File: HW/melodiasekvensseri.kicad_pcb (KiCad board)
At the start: 2 copper layers, 60.6 x 110 mm, 58 parts, among them IC1 74LS138, J1 Conn_02x05_Odd_Even, J2 Clock_In, J3 Gate_Out, J4 CV_Out, J5 Conn_02x03_Odd_Even, J6 Conn_01x04, U1 TLV2372IP

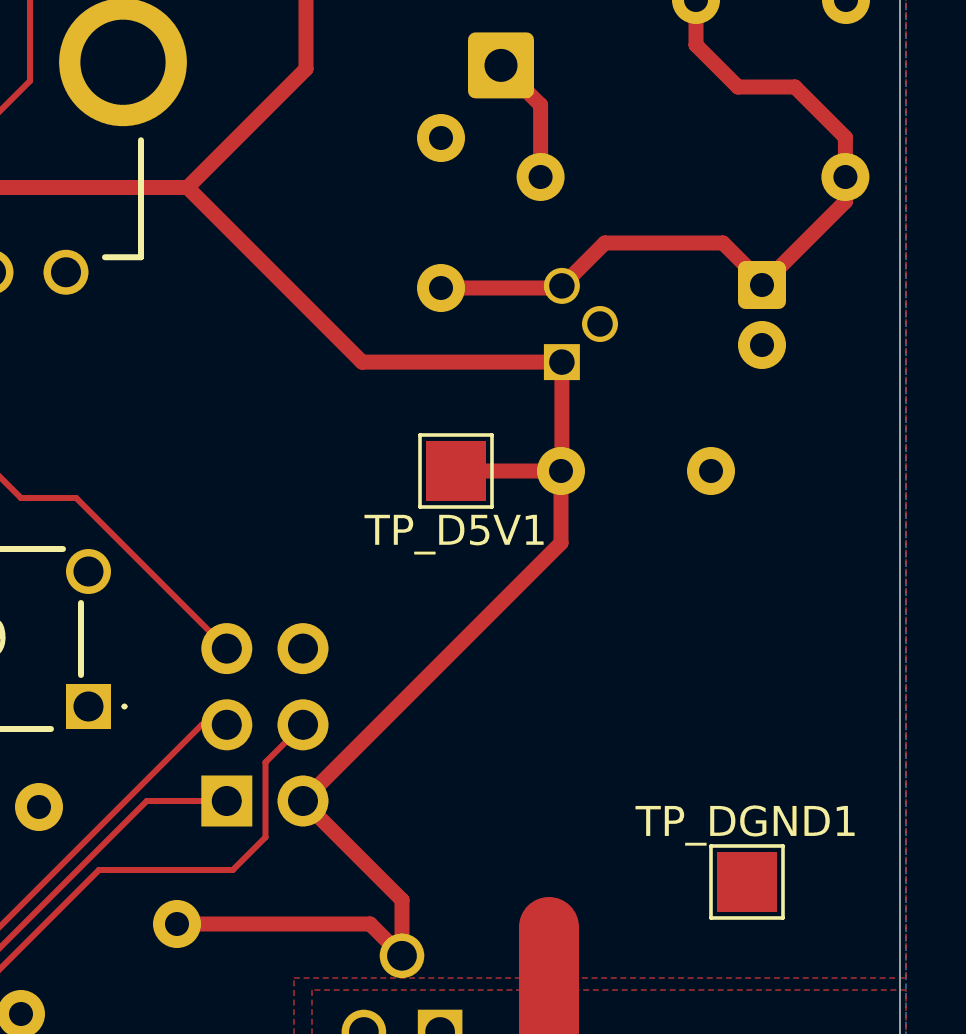
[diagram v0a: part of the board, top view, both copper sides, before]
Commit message: Panel clearances, switched REG1, added test code
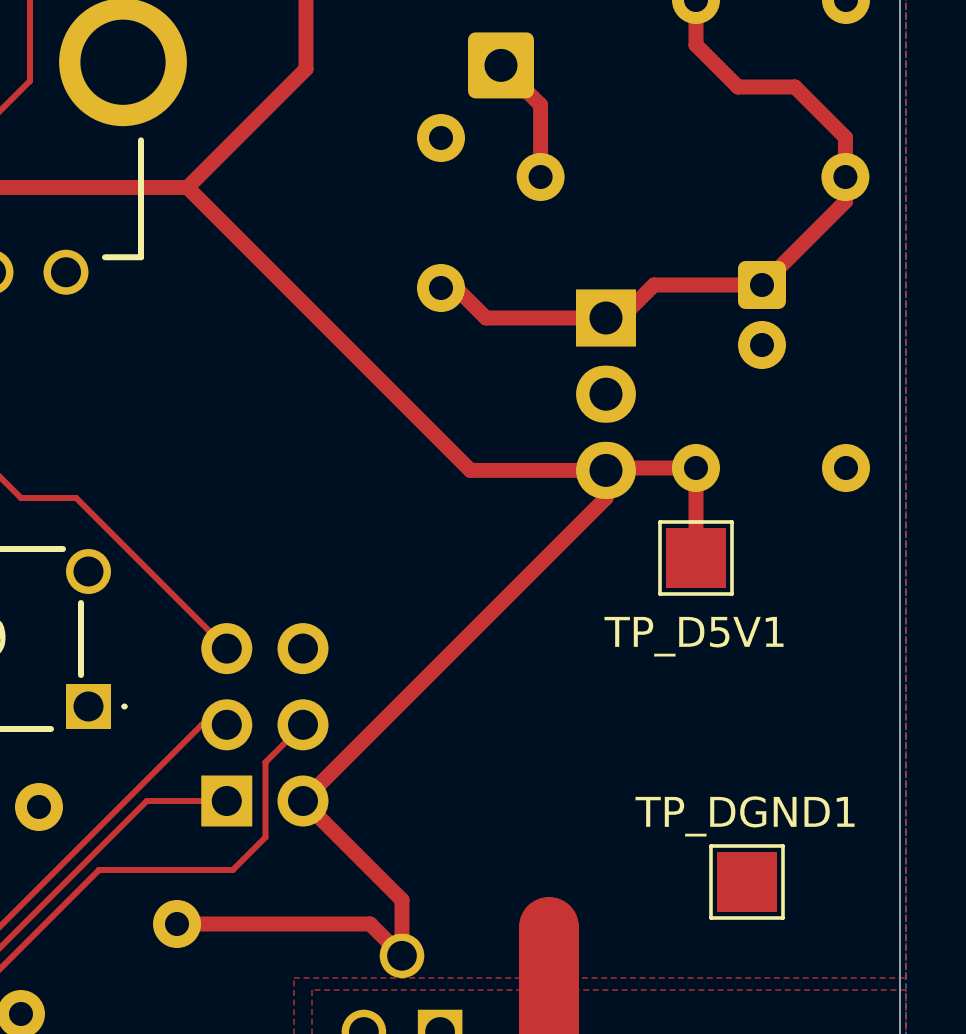
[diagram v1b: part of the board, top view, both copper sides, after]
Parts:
- REG1: footprint Project_Libraries:L78L05ACZ -> Package_TO_SOT_THT:TO-220-3_Vertical
- moved TP_D5V1 8.51 mm to (173.5, 85.5)
- moved C6 4.50 mm to (178.5, 82.5)
- moved REG1 2.08 mm to (170.5, 77.5), turned to -90 degrees
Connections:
- REG1 pad 1: D_+5V -> +12V
- REG1 pad 3: +12V -> D_+5V
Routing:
- net D_+5V: track 230.2 -> 232.7 mm

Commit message: Updated REG1 model name
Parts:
- REG1: value L78L05ACZ -> LM78M05
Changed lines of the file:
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@@
 			)
 		)
-		(property "Value" "L78L05ACZ"
-			(at 2.54 -2.2 90)
+		(property "Value" "LM78M05"
+			(at 4 2.5 90)
 			(layer "B.Fab")
 			(effects

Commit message: Removed CV_OUT diodes, filtering cap added
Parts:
- removed D4, D5: 1N4148, Diode_THT:D_DO-35_SOD27_P7.62mm_Horizontal
- added C15: 100n, Capacitor_THT:C_Disc_D5.0mm_W2.5mm_P5.00mm, B.Cu at (133.3, 97.7)
- TP_AGND1: footprint TestPoint:TestPoint_Pad_2.0x2.0mm -> TestPoint:TestPoint_THTPad_2.0x2.0mm_Drill1.0mm
- TP_CV_OUT1: renamed from TP_DAC_OUT1; footprint TestPoint:TestPoint_Pad_2.0x2.0mm -> TestPoint:TestPoint_THTPad_2.0x2.0mm_Drill1.0mm
- moved TP_A5V1 4.56 mm to (163.8, 120.7)
- moved TP_CV_OUT1 3.24 mm to (161.5, 129.8)
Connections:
- TP_CV_OUT1 pad 1: Net-(DAC1-VOUT) -> CV_Out
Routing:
- net Net-(DAC1-VOUT): track 25.2 -> 8.25 mm
- net A_+5V: track 58.8 -> 51.2 mm
- net CV_Out: track 32.1 -> 34.7 mm
- net D_+5V: track 232.7 -> 233.3 mm

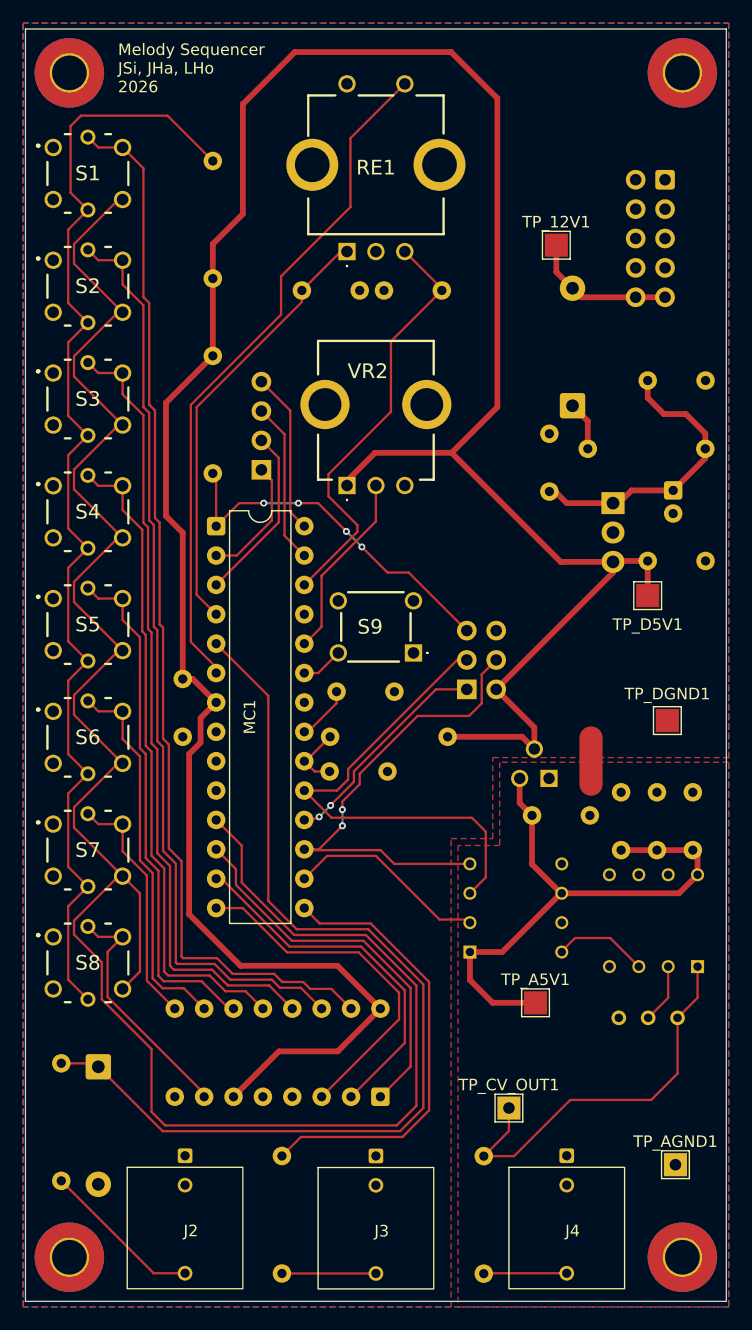
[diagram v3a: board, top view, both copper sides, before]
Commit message: Some resistor footprints changed
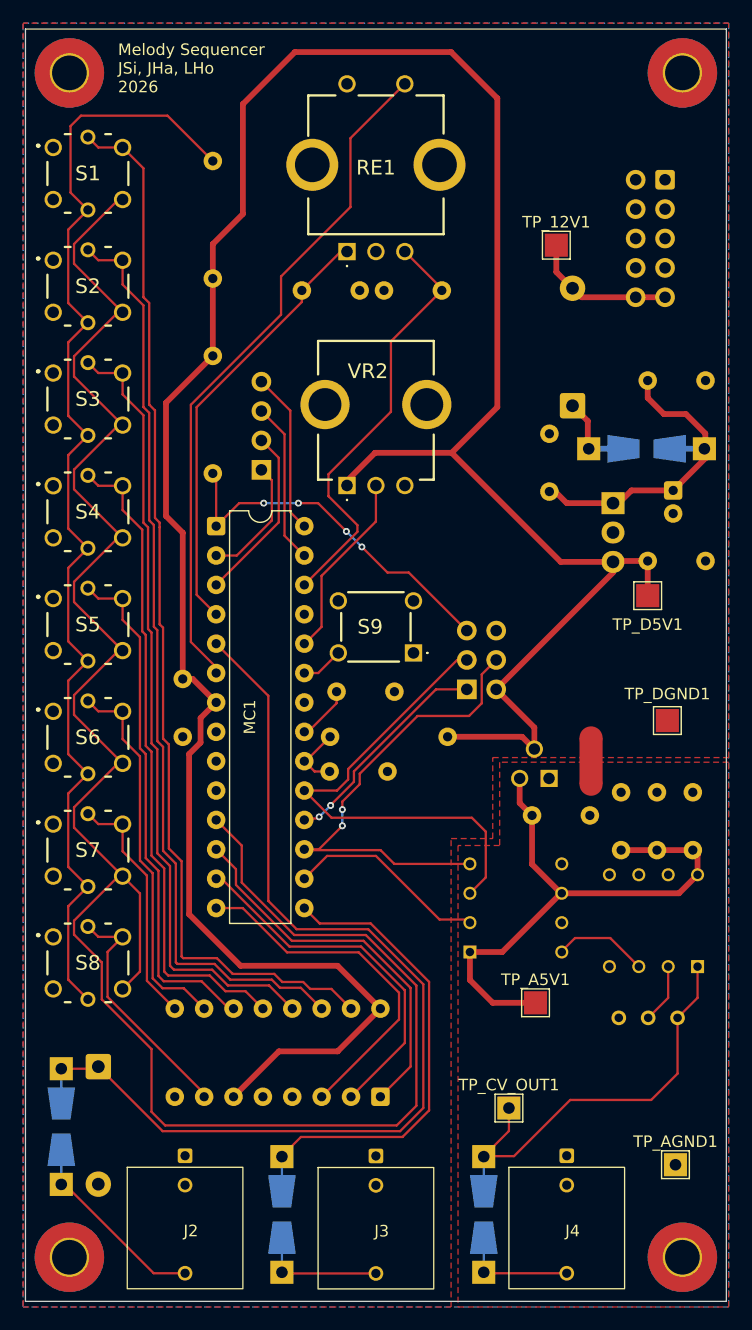
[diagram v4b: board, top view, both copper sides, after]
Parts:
- removed D3: 1N4733A, Diode_THT:D_DO-41_SOD81_P10.16mm_Horizontal
- added D2: 1N4733A, Diode_THT:D_DO-41_SOD81_P10.16mm_Horizontal, B.Cu at (126.0, 126.2)
- R1, R4, R5, R6: footprint Resistor_THT:R_Axial_DIN0207_L6.3mm_D2.5mm_P10.16mm_Horizontal -> Resistors_Universal.pretty-master:Resistor_SMD+THTuniversal_0805to1206_RM10_HandSoldering_RevA_Date25Jun2010
- moved R6 5.12 mm to (159.3, 139.0)
- moved R5 5.10 mm to (141.9, 139.0)
- moved R1 5.08 mm to (173.4, 72.8)
- moved R4 4.69 mm to (122.8, 131.4)
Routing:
- net CLK_IN: track 85.3 -> 88.7 mm
- net Net-(J4-PadT): track 7.14 -> 10.1 mm
- net Net-(J3-PadT): track 8.12 -> 11.1 mm
- net CV_Out: track 34.7 -> 37.7 mm
- net +12V: track 25.4 -> 28.4 mm
- net Net-(J2-PadT): track 14.0 -> 17.0 mm
- net Net-(D1-K): track 4.27 -> 7.27 mm
- net GATE_OUT: track 38.9 -> 41.9 mm

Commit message: REG2 changed, grounding fixes, routing changes
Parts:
- removed C7: 10u, Capacitor_THT:C_Disc_D5.0mm_W2.5mm_P5.00mm
- removed REF** (x4): MountingHole_3mm_Pad_TopBottom, MountingHole:MountingHole_3mm_Pad_TopBottom
- added C16: 100n, Capacitor_THT:C_Disc_D5.0mm_W2.5mm_P5.00mm, B.Cu at (166.5, 114.5)
- added C17: 330n, Capacitor_THT:C_Disc_D5.0mm_W2.5mm_P5.00mm, B.Cu at (166.5, 104.5)
- added H1: MountingHole, MountingHole:MountingHole_3.2mm_M3, F.Cu at (123.5, 40.3)
- added H2: MountingHole, MountingHole:MountingHole_3.2mm_M3, F.Cu at (176.5, 40.3)
- added H3: MountingHole, MountingHole:MountingHole_3.2mm_M3, F.Cu at (123.5, 142.7)
- added H4: MountingHole, MountingHole:MountingHole_3.2mm_M3, F.Cu at (176.5, 142.7)
- REG2: value MCP1700-5002E_TO -> L78L05ACZ; footprint Project_Libraries:TO127P254X495-3 -> Project_Libraries:L78L05ACZ
- TP_AGND1, TP_CV_OUT1: footprint TestPoint:TestPoint_THTPad_2.0x2.0mm_Drill1.0mm -> TestPoint:TestPoint_THTPad_1.5x1.5mm_Drill0.7mm
- moved REG2 12.1 mm to (164.1, 110.8)
- moved C5 11.3 mm to (163.3, 82.7), turned to 90 degrees
- moved TP_A5V1 10.2 mm to (161.0, 130.5)
- moved DAC1 9.00 mm to (162.1, 121.5)
- moved TP_CV_OUT1 8.51 mm to (170.0, 129.5), turned to 90 degrees
- moved TP_AGND1 6.19 mm to (172.5, 129.5), turned to -90 degrees
- moved R3 2.90 mm to (133.0, 58.1)
- moved C6 2.21 mm to (176.3, 82.7)
- moved REG1 2.21 mm to (168.3, 77.7)
- moved TP_D5V1 2.21 mm to (171.3, 85.7)
- moved J5 2.06 mm to (157.9, 91.5)
- moved R1 1.90 mm to (171.5, 72.8)
- moved R7 0.90 mm to (135.0, 74.9)
- moved C13 0.45 mm to (152.0, 94.0)
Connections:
- REG2 pad 1: A_GND -> A_+5V
- REG2 pad 2: D_+5V -> A_GND
- REG2 pad 3: A_+5V -> +12V
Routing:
- net D_+5V: track 233.3 -> 169.9 mm
- net +12V: track 28.4 -> 66.7 mm
- net D_GND: track 0.00 -> 31.7 mm, vias 0 -> 30
- net CV_Out: track 37.7 -> 30.7 mm
- net SPI_SCK: track 42.3 -> 47.7 mm, vias 0 -> 2
- net SPI_MOSI: track 41.4 -> 45.8 mm
- net DAC_CS: track 17.6 -> 21.1 mm
- net Net-(DAC1-VOUT): track 8.25 -> 11.2 mm
- net Net-(S1-A): track 100.3 -> 97.4 mm
- net Net-(IC1-O3): track 56.7 -> 54.3 mm
- net Net-(IC1-O2): track 68.4 -> 66.2 mm
- net Net-(IC1-O1): track 80.2 -> 78.1 mm
- net A_+5V: track 51.2 -> 49.2 mm
- net Net-(IC1-O0): track 92.0 -> 90.0 mm
- net Net-(IC1-O4): track 44.6 -> 42.6 mm
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- added copper zone on B.Cu, net A_GND

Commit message: Cleanup traces
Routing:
- net +12V: track 66.7 -> 65.6 mm
- net ENC_B: track 37.8 -> 36.9 mm
- net Net-(MC1-AREF): track 4.74 -> 3.92 mm
- net Net-(D1-K): track 6.93 -> 6.22 mm
- net ENC_A: track 39.1 -> 38.5 mm
- net ENC_S: track 60.2 -> 59.7 mm
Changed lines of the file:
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@@
 		(capping no)
 		(filling no)
-		(zone_defaults)
 		(pcbplotparams
 			(layerselection 0x00000000_00000000_55555555_575555ff)
@@
 	(segment
 		(start 149.675 73.4)
-		(end 156.3 73.4)
-		(width 0.5)
-		(layer "F.Cu")
-		(net "D_+5V")
-	)
-	(segment
-		(start 171.22 82.78)
-		(end 171.3 82.7)
+		(end 156.4 73.4)
 		(width 0.5)
 		(layer "F.Cu")
@@
 	)
 	(segment
-		(start 156.4 73.4)
-		(end 156.3 73.4)
-		(width 0.5)
-		(layer "F.Cu")
-		(net "D_+5V")
-	)
-	(segment
 		(start 149.675 67.775)
 		(end 149.675 73.4)
@@
 	)
 	(segment
-		(start 143.81 89.65)
-		(end 143.85 89.65)
-		(width 0.2)
-		(layer "F.Cu")
-		(net "TEMPO")
-	)
-	(segment
 		(start 152.5 111)
 		(end 152.373789 111)
@@
 	)
 	(segment
-		(start 147.5 55.75)
-		(end 146.963132 55.75)
-		(width 0.2)
-		(layer "F.Cu")
-		(net "ENC_A")
-	)
-	(segment
 		(start 133.65 72.25)
 		(end 133.65 84.57)
@@
 	)
 	(segment
-		(start 155.7 58.95)
-		(end 155.7 59.113132)
-		(width 0.2)
-		(layer "F.Cu")
-		(net "ENC_B")
-	)
-	(segment
 		(start 152.5 55.75)
 		(end 155.7 58.95)
@@
 	)
 	(segment
-		(start 152.95 55.263132)
-		(end 152.2 55.263132)
-		(width 0.2)
-		(layer "F.Cu")
-		(net "ENC_B")
-	)
-	(segment
 		(start 143.81 84.57)
 		(end 148.4 79.98)
@@
 		(net "ENC_S")
 	)
-	(segment
-		(start 136.19 91.69)
-		(end 136.19 92.19)
-		(width 0.2)
-		(layer "F.Cu")
-		(net "ENC_S")
-	)
 	(via
 		(at 137.3 62.7)
@@
 	)
 	(segment
-		(start 125.82126 126.39874)
-		(end 126 126.22)
-		(width 0.2)
-		(layer "F.Cu")
-		(net "CLK_IN")
-	)
-	(segment
 		(start 143.146566 114.33946)
 		(end 142 113.192894)
@@
 	)
 	(segment
-		(start 143.84 110)
-		(end 143.81 109.97)
-		(width 0.2)
-		(layer "F.Cu")
-		(net "DAC_CS")
-	)
-	(segment
 		(start 155.5 119)
 		(end 148 111.5)
@@
 	)
 	(segment
-		(start 160.830469 89)
-		(end 160.4 89)
-		(width 0.2)
-		(layer "F.Cu")
-		(net "SPI_MOSI")
-	)
-	(segment
 		(start 163.5 91.702083)
 		(end 163.5 94)
@@
 	)
 	(segment
-		(start 143.934975 105.014975)
-		(end 143.81 104.89)
-		(width 0.2)
-		(layer "F.Cu")
-		(net "SPI_MISO")
-	)
-	(segment
 		(start 148.5 102)
 		(end 148.5 101)
@@
 	)
 	(segment
-		(start 157.86 91.64)
-		(end 157.86 91.54)
-		(width 0.2)
-		(layer "F.Cu")
-		(net "SPI_MISO")
-	)
-	(segment
 		(start 146.5 104)
 		(end 148.5 102)
@@
 	)
 	(segment
-		(start 158.13 120.23)
-		(end 158.13 120.13)
-		(width 0.2)
-		(layer "F.Cu")
-		(net "SPI_SCK")
-	)
-	(segment
 		(start 157 89)
 		(end 155.5 90.5)
@@
 	)
 	(segment
-		(start 143.93 99.81)
-		(end 143.81 99.81)
-		(width 0.2)
-		(layer "F.Cu")
-		(net "Net-(MC1-AVCC)")
-	)
-	(segment
-		(start 143.81 97.19)
-		(end 143.81 97.27)
-		(width 0.2)
-		(layer "F.Cu")
-		(net "Net-(MC1-AREF)")
-	)
-	(segment
-		(start 143.81 97.27)
-		(end 144.13 97.27)
-		(width 0.2)
-		(layer "F.Cu")
-		(net "Net-(MC1-AREF)")
-	)
-	(segment
-		(start 146.58 94.5)
-		(end 147 94.5)
-		(width 0.2)
-		(layer "F.Cu")
-		(net "Net-(MC1-AREF)")
-	)
-	(segment
 		(start 143.81 97.27)
 		(end 146.58 94.5)
@@
 	)
 	(segment
-		(start 122.8 136.093132)
-		(end 130.79 144.083132)
-		(width 0.2)
-		(layer "F.Cu")
-		(net "Net-(J2-PadT)")
-	)
-	(segment
-		(start 130.79 144.083132)
-		(end 133.5 144.083132)
-		(width 0.2)
-		(layer "F.Cu")
-		(net "Net-(J2-PadT)")
-	)
-	(segment
-		(start 122.8 133.39898)
-		(end 122.8 136.40126)
-		(width 0.2)
-		(layer "B.Cu")
-		(net "Net-(J2-PadT)")
-	)
-	(segment
 		(start 167.5 129.5)
 		(end 163.00126 133.99874)
@@
 	)
 	(segment
+		(start 122.8 136.093132)
+		(end 130.79 144.083132)
+		(width 0.2)
+		(layer "F.Cu")
+		(net "Net-(J2-PadT)")
+	)
+	(segment
+		(start 130.79 144.083132)
+		(end 133.5 144.083132)
+		(width 0.2)
+		(layer "F.Cu")
+		(net "Net-(J2-PadT)")
+	)
+	(segment
+		(start 122.8 133.39898)
+		(end 122.8 136.40126)
+		(width 0.2)
+		(layer "B.Cu")
+		(net "Net-(J2-PadT)")
+	)
+	(segment
 		(start 137.296026 120.243689)
 		(end 137.296026 121.203132)
@@
 	)
 	(segment
-		(start 175.7 76.4)
-		(end 176.3 76.4)
-		(width 0.5)
-		(layer "F.Cu")
-		(net "+12V")
-	)
-	(segment
 		(start 173.5 78.1)
 		(end 173.5 89.2)
@@
 	)
 	(segment
-		(start 175.7 76.4)
-		(end 175.2 76.4)
-		(width 0.5)
-		(layer "F.Cu")
-		(net "+12V")
-	)
-	(segment
 		(start 173.5 66.9)
 		(end 173.5 68.4)
@@
 	)
 	(segment
-		(start 172.73 117.77)
-		(end 172.73 117.57)
-		(width 0.2)
-		(layer "F.Cu")
-		(net "Net-(DAC1-VOUT)")
-	)
-	(segment
 		(start 169 123.5)
 		(end 169 121.5)
@@
 	)
 	(segment
-		(start 167 72.29874)
-		(end 166.49874 72.8)
-		(width 0.5)
-		(layer "F.Cu")
-		(net "Net-(D1-K)")
-	)
-	(segment

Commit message: Added ground via, small changes
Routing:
- net D_GND: track 31.7 -> 33.5 mm, vias 30 -> 32
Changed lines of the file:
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@@
+	)
+	(segment
+		(start 140 125.31105)
+		(end 139.905525 125.405525)
+		(width 0.2)
+		(layer "F.Cu")
+		(net "D_GND")
 	)
 	(segment
@@
 	)
 	(via
+		(at 141.107607 126.607607)
+		(size 0.6)
+		(drill 0.3)
+		(layers "F.Cu" "B.Cu")
+		(net "D_GND")
+	)
+	(via
 		(at 139.5 79.5)
 		(size 0.6)
@@
 	(via
 		(at 152.373789 111)
+		(size 0.6)
+		(drill 0.3)
+		(layers "F.Cu" "B.Cu")
+		(net "D_GND")
+	)
+	(via
+		(at 139.905525 125.405525)
 		(size 0.6)
 		(drill 0.3)
@@
 		(width 0.2)
 		(layer "B.Cu")
+		(net "D_GND")
+	)
+	(segment
+		(start 139.905525 125.405525)
+		(end 141.107607 126.607607)
+		(width 0.2)
+		(layer "B.Cu")
